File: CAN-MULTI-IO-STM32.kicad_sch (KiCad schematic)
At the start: 63 parts, among them J1 H GND L, J2 TERM, J3 USART1, J5 PWR IN, U1 STM32L433RCT3, U2 MCP2562-E-SN, U3 LMR54410, U4 ADS1015IDGS, U5 PCA9537, U6 TCA9511

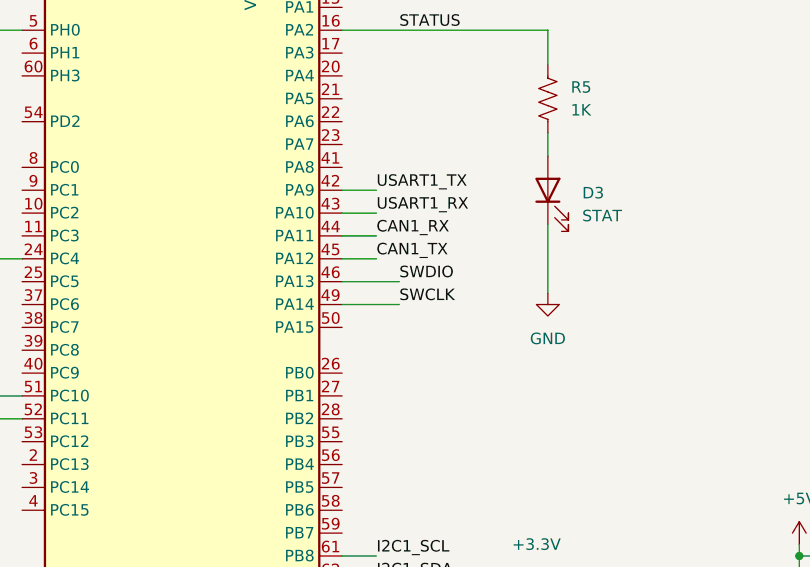
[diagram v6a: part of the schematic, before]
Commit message: first pass layout complete
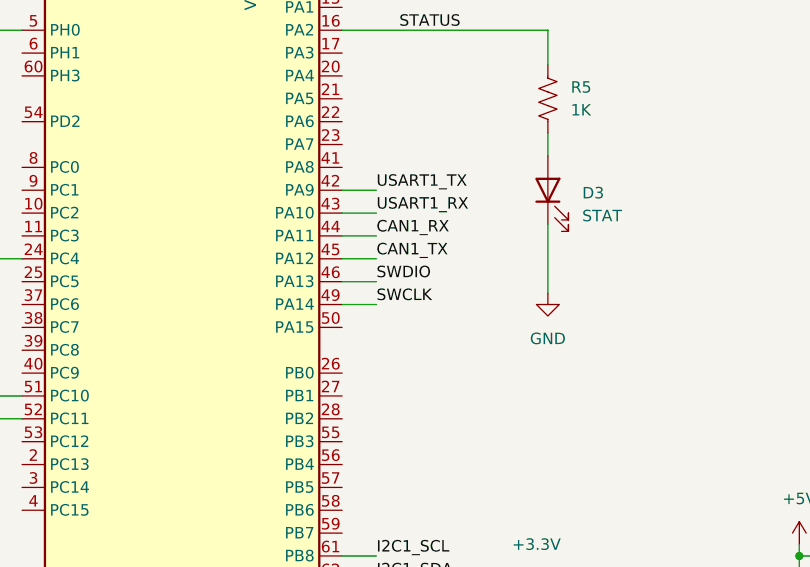
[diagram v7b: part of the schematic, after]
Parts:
- ANA_IN1, GPIO_CON1: footprint TerminalBlock_TE-Connectivity:TerminalBlock_TE_282834-6_1x06_P2.54mm_Horizontal -> TerminalBlock_Phoenix:TerminalBlock_Phoenix_MPT-0,5-6-2.54_1x06_P2.54mm_Horizontal
- J3: footprint PCM_SparkFun-Connector:1x04_P2.54mm_Locking -> Connector_PinHeader_2.54mm:PinHeader_1x04_P2.54mm_Vertical
- SWD1: footprint PCM_SparkFun-Connector:1x05_P2.54mm_Locking -> Connector_PinHeader_2.54mm:PinHeader_1x05_P2.54mm_Vertical
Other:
- title: CAN-STM32L433 -> CAN-MULTI-IO-STM32
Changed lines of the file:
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@@
 	(paper "USLegal")
 	(title_block
-		(title "CAN-STM32L433")
-		(date "2026-01-13")
+		(title "CAN-MULTI-IO-STM32")
+		(date "2026-01-21")
 		(company "Gordon McLellan")
-		(comment 1 "CAN Bus Multi-IO Board STM32")
+		(comment 1 "CAN Bus Multi-IO Module STM32")
 	)
 	(junction
@@
 	(wire
 		(pts
-			(xy 157.48 96.52) (xy 163.83 96.52)
+			(xy 157.48 96.52) (xy 161.29 96.52)
 		)
 		(stroke
@@
 	(wire
 		(pts
-			(xy 157.48 93.98) (xy 163.83 93.98)
+			(xy 157.48 93.98) (xy 161.29 93.98)
 		)
 		(stroke
@@
 	)
 	(label "SWCLK"
-		(at 163.83 96.52 0)
+		(at 161.29 96.52 0)
 		(effects
 			(font
@@
 	)
 	(label "SWDIO"
-		(at 163.83 93.98 0)
+		(at 161.29 93.98 0)
 		(effects
 			(font
@@
 			)
 		)
-		(property "Footprint" "TerminalBlock_TE-Connectivity:TerminalBlock_TE_282834-6_1x06_P2.54mm_Horizontal"
+		(property "Footprint" "TerminalBlock_Phoenix:TerminalBlock_Phoenix_MPT-0,5-6-2.54_1x06_P2.54mm_Horizontal"
 			(at 260.35 133.35 0)
 			(effects
@@
 			)
 		)
-		(property "Footprint" "PCM_SparkFun-Connector:1x05_P2.54mm_Locking"
+		(property "Footprint" "Connector_PinHeader_2.54mm:PinHeader_1x05_P2.54mm_Vertical"
 			(at 312.42 82.55 0)
 			(effects
@@
 			)
 		)
-		(property "Footprint" "PCM_SparkFun-Connector:1x04_P2.54mm_Locking"
+		(property "Footprint" "Connector_PinHeader_2.54mm:PinHeader_1x04_P2.54mm_Vertical"
 			(at 314.96 153.67 0)
 			(effects
@@
 			)
 		)
-		(property "Footprint" "TerminalBlock_TE-Connectivity:TerminalBlock_TE_282834-6_1x06_P2.54mm_Horizontal"
+		(property "Footprint" "TerminalBlock_Phoenix:TerminalBlock_Phoenix_MPT-0,5-6-2.54_1x06_P2.54mm_Horizontal"
 			(at 260.35 86.36 0)
 			(effects

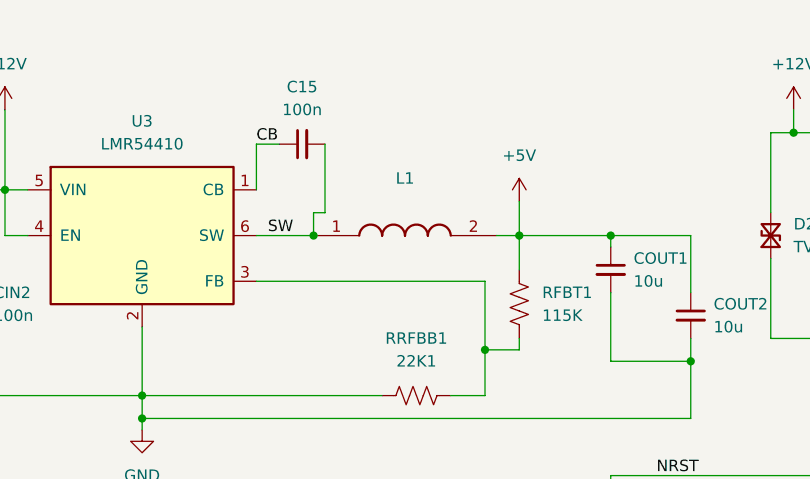
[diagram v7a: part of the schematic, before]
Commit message: fixed issue with incorrect inductor
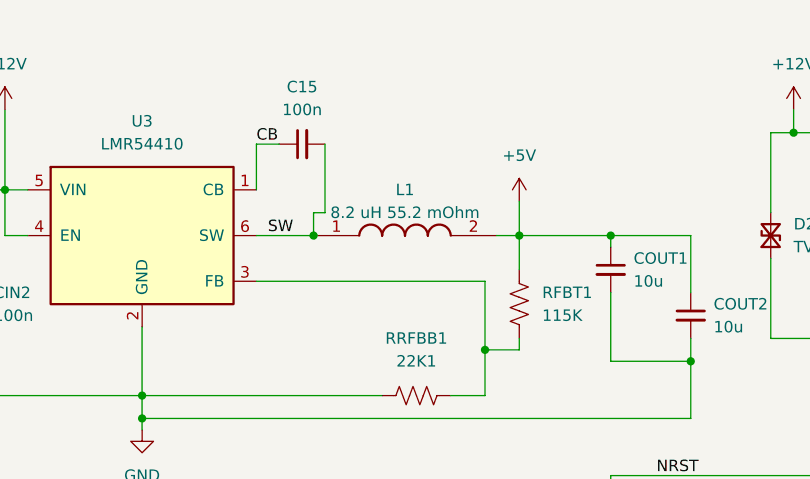
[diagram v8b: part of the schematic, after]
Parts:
- removed L1: VLS5045EX-100M-H, VLS5045EX330M, symbol SamacSys_Parts:VLS5045EX-100M-H
- added L1: 8.2 uH 55.2 mOhm, SRP5030HMT2R2M, symbol SamacSys_Parts:SRP5030HMT-8R2M
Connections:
- net +5V: now also L1.2
- net SW: now also L1.1
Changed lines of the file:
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@@
 	)
 	(junction
+		(at 59.69 34.29)
+		(diameter 0)
+		(color 0 0 0 0)
+	)
+	(junction
 		(at 191.77 36.83)
 		(diameter 0)
@@
 	)
 	(junction
-		(at 59.69 34.29)
-		(diameter 0)
-		(color 0 0 0 0)
-	)
-	(junction
 		(at 223.52 20.32)
 		(diameter 0)
@@
 	)
 	(symbol
-		(lib_id "SamacSys_Parts:VLS5045EX-100M-H")
-		(at 59.69 34.29 0)
-		(unit 1)
-		(exclude_from_sim no)
-		(in_bom yes)
-		(on_board yes)
-		(dnp no)
-		(fields_autoplaced yes)
-		(property "Reference" "L1"
-			(at 69.85 27.94 0)
-			(effects
-				(font
-					(size 1.27 1.27)
-				)
-			)
-		)
-		(property "Value" "VLS5045EX-100M-H"
-			(at 69.85 30.48 0)
-			(effects
-				(font
-					(size 1.27 1.27)
-				)
-				(hide yes)
-			)
-		)
-		(property "Footprint" "VLS5045EX330M"
-			(at 76.2 130.48 0)
-			(effects
-				(font
-					(size 1.27 1.27)
-				)
-				(justify left top)
-				(hide yes)
-			)
-		)
-		(property "Datasheet" "https://product.tdk.com/system/files/dam/doc/product/inductor/inductor/smd/catalog/inductor_automotive_power_vls5045ex-h_en.pdf"
-			(at 76.2 230.48 0)
-			(effects
-				(font
-					(size 1.27 1.27)
-				)
-				(justify left top)
-				(hide yes)
-			)
-		)
-		(property "Description" "SMD / SMT Inductors (Coils), L=10?H, L x W x T :"
-			(at 59.69 34.29 0)
-			(effects
-				(font
-					(size 1.27 1.27)
-				)
-				(hide yes)
-			)
-		)
-		(property "Height" "4"
-			(at 76.2 430.48 0)
-			(effects
-				(font
-					(size 1.27 1.27)
-				)
-				(justify left top)
-				(hide yes)
-			)
-		)
-		(property "Mouser Part Number" "810-VLS5045EX-100M-H"
-			(at 76.2 530.48 0)
-			(effects
-				(font
-					(size 1.27 1.27)
-				)
-				(justify left top)
-				(hide yes)
-			)
-		)
-		(property "Mouser Price/Stock" "https://www.mouser.co.uk/ProductDetail/TDK/VLS5045EX-100M-H?qs=EBDBlbfErPxDDKYBGzjLDg%3D%3D"
-			(at 76.2 630.48 0)
-			(effects
-				(font
-					(size 1.27 1.27)
-				)
-				(justify left top)
-				(hide yes)
-			)
-		)
-		(property "Manufacturer_Name" "TDK"
-			(at 76.2 730.48 0)
-			(effects
-				(font
-					(size 1.27 1.27)
-				)
-				(justify left top)
-				(hide yes)
-			)
-		)
-		(property "Manufacturer_Part_Number" "VLS5045EX-100M-H"
-			(at 76.2 830.48 0)
-			(effects
-				(font
-					(size 1.27 1.27)
-				)
-				(justify left top)
-				(hide yes)
-			)
-		)
-		(pin "1"
-		)
-		(pin "2"
-		)
-		(instances
-			(project ""
-				(path "/807782eb-8307-4922-8e5a-50da44718f8e"
-					(reference "L1")
-					(unit 1)
-				)
-			)
-		)
-	)
-	(symbol
 		(lib_id "power:+5V")
 		(at 27.94 68.58 0)
@@
 					(unit 1)
 				)
+			)
+		)
+	)
+	(symbol
+		(lib_id "SamacSys_Parts:SRP5030HMT-8R2M")
+		(at 59.69 34.29 0)
+		(unit 1)
+		(exclude_from_sim no)
+		(in_bom yes)
+		(on_board yes)
+		(dnp no)
+		(fields_autoplaced yes)
+		(property "Reference" "L1"
+			(at 69.85 29.21 0)
+			(effects
+				(font
+					(size 1.27 1.27)
+				)
+			)
+		)
+		(property "Value" "8.2 uH 55.2 mOhm"
+			(at 69.85 31.75 0)
+			(effects
+				(font
+					(size 1.27 1.27)
+				)
+			)
+		)
+		(property "Footprint" "SRP5030HMT2R2M"
+			(at 76.2 130.48 0)
+			(effects
+				(font
+					(size 1.27 1.27)
+				)
+				(justify left top)
+				(hide yes)
+			)
+		)
+		(property "Datasheet" "https://www.bourns.com/docs/Product-Datasheets/SRP5030HMT.pdf"
+			(at 76.2 230.48 0)
+			(effects
+				(font
+					(size 1.27 1.27)
+				)
+				(justify left top)
+				(hide yes)
+			)
+		)
+		(property "Description" "Ind,5.2x5.6x2.8mm,8.2uH+/-20%,5.8A,shd"
+			(at 59.69 34.29 0)
+			(effects
+				(font
+					(size 1.27 1.27)
+				)
+				(hide yes)
+			)
+		)
+		(property "Height" "3"
+			(at 76.2 430.48 0)
+			(effects
+				(font
+					(size 1.27 1.27)
+				)
+				(justify left top)
+				(hide yes)
+			)
+		)
+		(property "Mouser Part Number" "SRP5030HMT-8R2M"
+			(at 76.2 530.48 0)
+			(effects
+				(font
+					(size 1.27 1.27)
+				)
+				(justify left top)
+				(hide yes)
+			)
+		)
+		(property "Mouser Price/Stock" ""
+			(at 76.2 630.48 0)
+			(effects
+				(font
+					(size 1.27 1.27)
+				)
+				(justify left top)
+				(hide yes)
+			)
+		)
+		(property "Manufacturer_Name" "Bourns"
+			(at 76.2 730.48 0)
+			(effects
+				(font
+					(size 1.27 1.27)
+				)
+				(justify left top)
+				(hide yes)
+			)
+		)
+		(property "Manufacturer_Part_Number" "SRP5030HMT-8R2M"
+			(at 76.2 830.48 0)
+			(effects
+				(font
+					(size 1.27 1.27)
+				)
+				(justify left top)
+				(hide yes)
+			)
+		)
+		(pin "1"
+		)
+		(pin "2"
+		)
+		(instances
+			(project ""
+				(path "/807782eb-8307-4922-8e5a-50da44718f8e"
+					(reference "L1")
+					(unit 1)
+				)
